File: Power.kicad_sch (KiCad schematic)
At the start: 21 parts, among them U601 HT7463A, U602 BD2243G, U603 MIC5504-3.3YM5

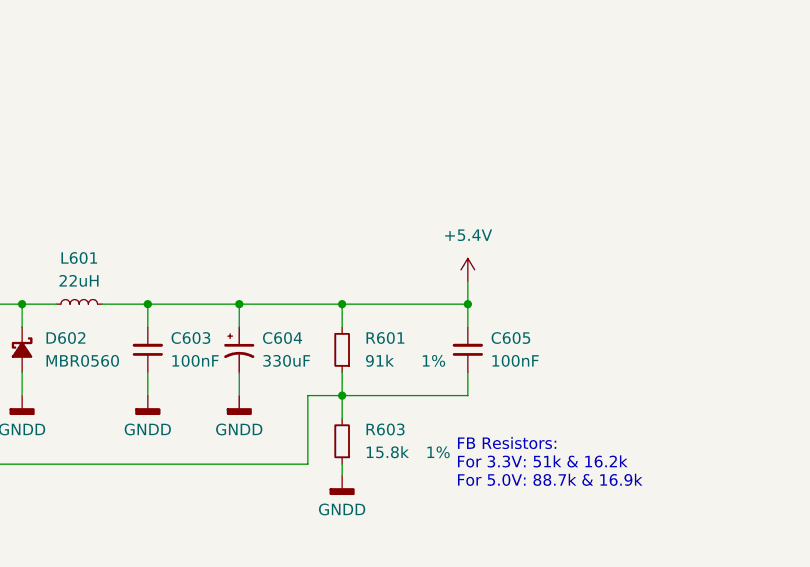
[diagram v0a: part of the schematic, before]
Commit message: Many more vias, improved some routing
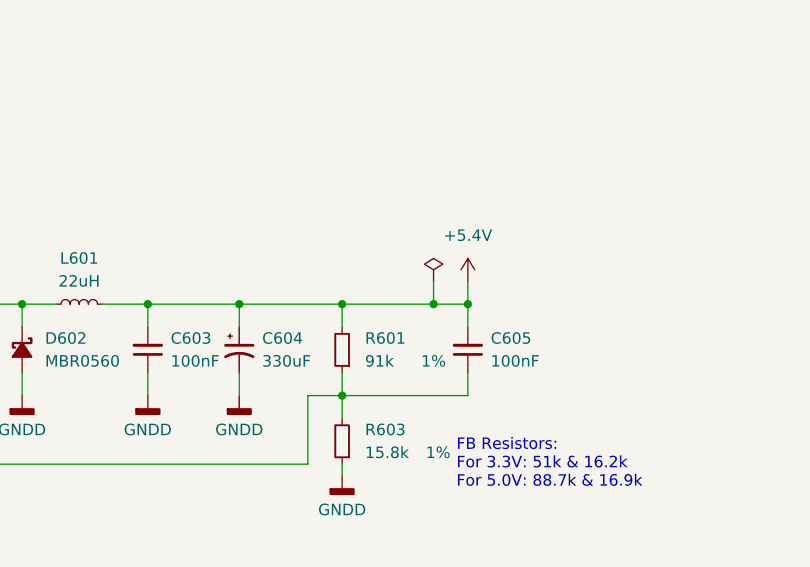
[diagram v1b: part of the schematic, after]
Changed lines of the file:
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@@
+	)
+	(junction
+		(at 173.99 55.88)
+		(diameter 0)
+		(color 0 0 0 0)
 	)
 	(junction
@@
 	(wire
 		(pts
+			(xy 173.99 53.34) (xy 173.99 55.88)
+		)
+		(stroke
+			(width 0)
+			(type default)
+		)
+	)
+	(wire
+		(pts
 			(xy 67.31 95.25) (xy 67.31 90.17)
 		)
@@
 	(wire
 		(pts
+			(xy 173.99 55.88) (xy 177.8 55.88)
+		)
+		(stroke
+			(width 0)
+			(type solid)
+		)
+	)
+	(wire
+		(pts
 			(xy 114.3 106.68) (xy 114.3 109.22)
 		)
@@
 	(wire
 		(pts
-			(xy 163.83 55.88) (xy 177.8 55.88)
+			(xy 163.83 55.88) (xy 173.99 55.88)
 		)
 		(stroke
@@
 					(unit 1)
 				)
+			)
+		)
+	)
+	(symbol
+		(lib_id "power:PWR_FLAG")
+		(at 173.99 53.34 0)
+		(unit 1)
+		(exclude_from_sim no)
+		(in_bom yes)
+		(on_board yes)
+		(dnp no)
+		(fields_autoplaced yes)
+		(property "Reference" "#FLG0601"
+			(at 173.99 51.435 0)
+			(effects
+				(font
+					(size 1.27 1.27)
+				)
+				(hide yes)
+			)
+		)
+		(property "Value" "PWR_FLAG"
+			(at 173.99 48.26 0)
+			(effects
+				(font
+					(size 1.27 1.27)
+				)
+				(hide yes)
+			)
+		)
+		(property "Footprint" ""
+			(at 173.99 53.34 0)
+			(effects
+				(font
+					(size 1.27 1.27)
+				)
+				(hide yes)
+			)
+		)
+		(property "Datasheet" "~"
+			(at 173.99 53.34 0)
+			(effects
+				(font
+					(size 1.27 1.27)
+				)
+				(hide yes)
+			)
+		)
+		(property "Description" "Special symbol for telling ERC where power comes from"
+			(at 173.99 53.34 0)
+			(effects
+				(font
+					(size 1.27 1.27)
+				)
+				(hide yes)
+			)
+		)
+		(pin "1"
+		)
+		(instances
+			(project "ZFTuner"
+				(path "/fdb95973-bff7-44bf-8fa0-11fcc1e3382d/4f4b3f21-035d-41e9-bc50-b9de10321df3"
+					(reference "#FLG0601")
+					(unit 1)
+				)

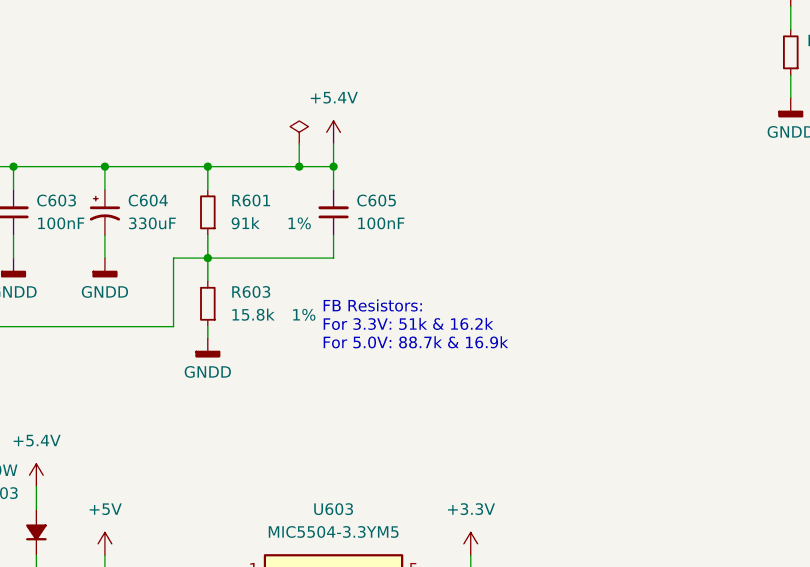
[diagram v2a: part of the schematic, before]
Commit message: Removed unclear text in schematic. Some minor PCB routing improvments. Added name and revision silkscreen
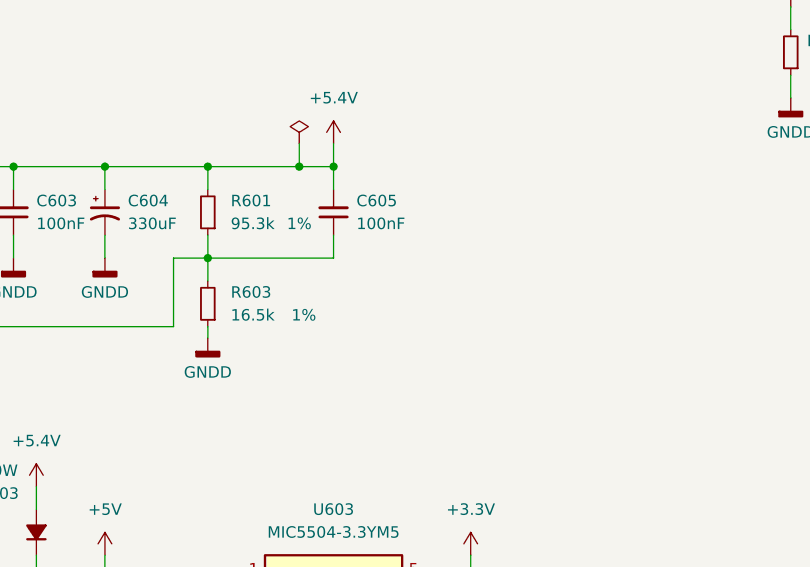
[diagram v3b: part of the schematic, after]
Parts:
- R601: value 91k -> 95.3k
- R603: value 15.8k -> 16.5k
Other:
- note removed: "FB Resistors: For 3.3V: 51k & 16.2k For 5.0V: 88.7k & 16.9k"
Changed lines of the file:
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@@
-		)
-	)
-	(text "FB Resistors:\nFor 3.3V: 51k & 16.2k\nFor 5.0V: 88.7k & 16.9k"
-		(exclude_from_sim no)
-		(at 176.53 76.454 0)
-		(effects
-			(font
-				(size 1.27 1.27)
-			)
-			(justify left bottom)
 		)
 	)
@@
 			)
 		)
-		(property "Value" "91k"
+		(property "Value" "95.3k"
 			(at 166.37 62.2299 0)
 			(effects
@@
 			)
 		)
-		(property "Value" "15.8k"
+		(property "Value" "16.5k"
 			(at 166.37 72.3899 0)
 			(effects

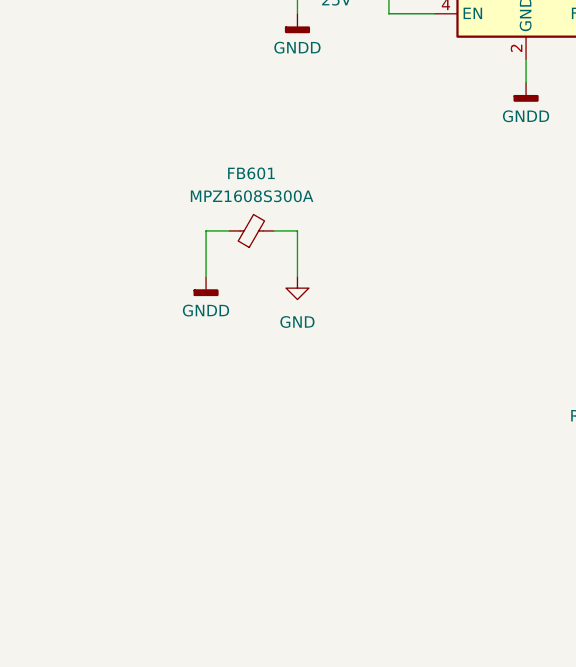
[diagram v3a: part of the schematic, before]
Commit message: Improved grounding
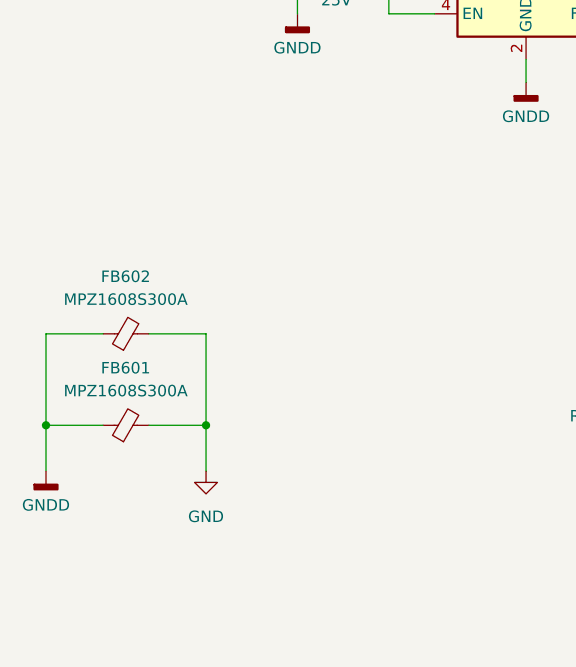
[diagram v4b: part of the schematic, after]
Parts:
- added FB602: MPZ1608S300A, Inductor_SMD:L_0603_1608Metric, symbol Device:FerriteBead_Small
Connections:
- net GND: now also FB602.2
- net GNDD: now also FB602.1
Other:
- moved on the sheet: FB601
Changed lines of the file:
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@@
 	)
 	(junction
+		(at 67.31 111.76)
+		(diameter 0)
+		(color 0 0 0 0)
+	)
+	(junction
 		(at 163.83 66.04)
 		(diameter 0)
@@
 	)
 	(junction
+		(at 49.53 111.76)
+		(diameter 0)
+		(color 0 0 0 0)
+	)
+	(junction
 		(at 87.63 55.88)
 		(diameter 0)
@@
 	(wire
 		(pts
+			(xy 49.53 111.76) (xy 49.53 101.6)
+		)
+		(stroke
+			(width 0)
+			(type default)
+		)
+	)
+	(wire
+		(pts
 			(xy 177.8 53.34) (xy 177.8 55.88)
 		)
@@
 	(wire
 		(pts
-			(xy 67.31 95.25) (xy 67.31 90.17)
+			(xy 49.53 116.84) (xy 49.53 111.76)
 		)
 		(stroke
@@
 	(wire
 		(pts
-			(xy 74.93 90.17) (xy 77.47 90.17)
+			(xy 67.31 101.6) (xy 60.96 101.6)
+		)
+		(stroke
+			(width 0)
+			(type default)
+		)
+	)
+	(wire
+		(pts
+			(xy 60.96 111.76) (xy 67.31 111.76)
 		)
 		(stroke
@@
 	(wire
 		(pts
+			(xy 49.53 101.6) (xy 55.88 101.6)
+		)
+		(stroke
+			(width 0)
+			(type default)
+		)
+	)
+	(wire
+		(pts
 			(xy 120.65 60.96) (xy 123.19 60.96)
 		)
@@
 	(wire
 		(pts
-			(xy 77.47 90.17) (xy 77.47 95.25)
+			(xy 67.31 111.76) (xy 67.31 116.84)
 		)
 		(stroke
@@
 	(wire
 		(pts
+			(xy 67.31 111.76) (xy 67.31 101.6)
+		)
+		(stroke
+			(width 0)
+			(type default)
+		)
+	)
+	(wire
+		(pts
 			(xy 128.27 63.5) (xy 128.27 66.04)
 		)
@@
 	(wire
 		(pts
-			(xy 67.31 90.17) (xy 69.85 90.17)
+			(xy 49.53 111.76) (xy 55.88 111.76)
 		)
 		(stroke
@@
 	(symbol
 		(lib_id "power:GND")
-		(at 77.47 95.25 0)
+		(at 67.31 116.84 0)
 		(unit 1)
 		(exclude_from_sim no)
@@
 		(fields_autoplaced yes)
 		(property "Reference" "#PWR0613"
-			(at 77.47 101.6 0)
+			(at 67.31 123.19 0)
 			(effects
 				(font
@@
 		)
 		(property "Value" "GND"
-			(at 77.47 100.33 0)
+			(at 67.31 121.92 0)
 			(effects
 				(font
@@
 		)
 		(property "Footprint" ""
-			(at 77.47 95.25 0)
+			(at 67.31 116.84 0)
 			(effects
 				(font
@@
 		)
 		(property "Datasheet" ""
-			(at 77.47 95.25 0)
+			(at 67.31 116.84 0)
 			(effects
 				(font
@@
 		)
 		(property "Description" "Power symbol creates a global label with name \"GND\" , ground"
-			(at 77.47 95.25 0)
+			(at 67.31 116.84 0)
 			(effects
 				(font
@@
 	)
 	(symbol
+		(lib_id "Device:FerriteBead_Small")
+		(at 58.42 101.6 90)
+		(unit 1)
+		(exclude_from_sim no)
+		(in_bom yes)
+		(on_board yes)
+		(dnp no)
+		(fields_autoplaced yes)
+		(property "Reference" "FB602"
+			(at 58.3819 95.25 90)
+			(effects
+				(font
+					(size 1.27 1.27)
+				)
+			)
+		)
+		(property "Value" "MPZ1608S300A"
+			(at 58.3819 97.79 90)
+			(effects
+				(font
+					(size 1.27 1.27)
+				)
+			)
+		)
+		(property "Footprint" "Inductor_SMD:L_0603_1608Metric"
+			(at 58.42 103.378 90)
+			(effects
+				(font
+					(size 1.27 1.27)
+				)
+				(hide yes)
+			)
+		)
+		(property "Datasheet" "~"
+			(at 58.42 101.6 0)
+			(effects
+				(font
+					(size 1.27 1.27)
+				)
+				(hide yes)
+			)
+		)
+		(property "Description" "Ferrite bead, small symbol"
+			(at 58.42 101.6 0)
+			(effects
+				(font
+					(size 1.27 1.27)
+				)
+				(hide yes)
+			)
+		)
+		(pin "2"
+		)
+		(pin "1"
+		)
+		(instances
+			(project "ZFTuner"
+				(path "/fdb95973-bff7-44bf-8fa0-11fcc1e3382d/4f4b3f21-035d-41e9-bc50-b9de10321df3"
+					(reference "FB602")
+					(unit 1)
+				)
+			)
+		)
+	)
+	(symbol
 		(lib_id "power:GNDD")
 		(at 152.4 111.76 0)
@@
 	(symbol
 		(lib_id "power:GNDD")
-		(at 67.31 95.25 0)
+		(at 49.53 116.84 0)
 		(unit 1)
 		(exclude_from_sim no)
@@
 		(fields_autoplaced yes)
 		(property "Reference" "#PWR0612"
-			(at 67.31 101.6 0)
+			(at 49.53 123.19 0)
 			(effects
 				(font
@@
 		)
 		(property "Value" "GNDD"
-			(at 67.31 99.06 0)
+			(at 49.53 120.65 0)
 			(effects
 				(font
@@
 		)
 		(property "Footprint" ""
-			(at 67.31 95.25 0)
+			(at 49.53 116.84 0)
 			(effects
 				(font
@@
 		)
 		(property "Datasheet" ""
-			(at 67.31 95.25 0)
+			(at 49.53 116.84 0)
 			(effects
 				(font
@@
 		)
 		(property "Description" "Power symbol creates a global label with name \"GNDD\" , digital ground"
-			(at 67.31 95.25 0)
+			(at 49.53 116.84 0)
 			(effects
 				(font
@@
 	(symbol
 		(lib_id "Device:FerriteBead_Small")
-		(at 72.39 90.17 90)
+		(at 58.42 111.76 90)
 		(unit 1)
 		(exclude_from_sim no)
@@
 		(fields_autoplaced yes)
 		(property "Reference" "FB601"
-			(at 72.3519 83.82 90)
+			(at 58.3819 105.41 90)
 			(effects
 				(font
@@
 		)
 		(property "Value" "MPZ1608S300A"
-			(at 72.3519 86.36 90)
+			(at 58.3819 107.95 90)
 			(effects
 				(font
@@
 		)
 		(property "Footprint" "Inductor_SMD:L_0603_1608Metric"
-			(at 72.39 91.948 90)
+			(at 58.42 113.538 90)
 			(effects
 				(font
@@
 		)
 		(property "Datasheet" "~"
-			(at 72.39 90.17 0)
+			(at 58.42 111.76 0)
 			(effects
 				(font
@@
 		)
 		(property "Description" "Ferrite bead, small symbol"
-			(at 72.39 90.17 0)
+			(at 58.42 111.76 0)
 			(effects
 				(font

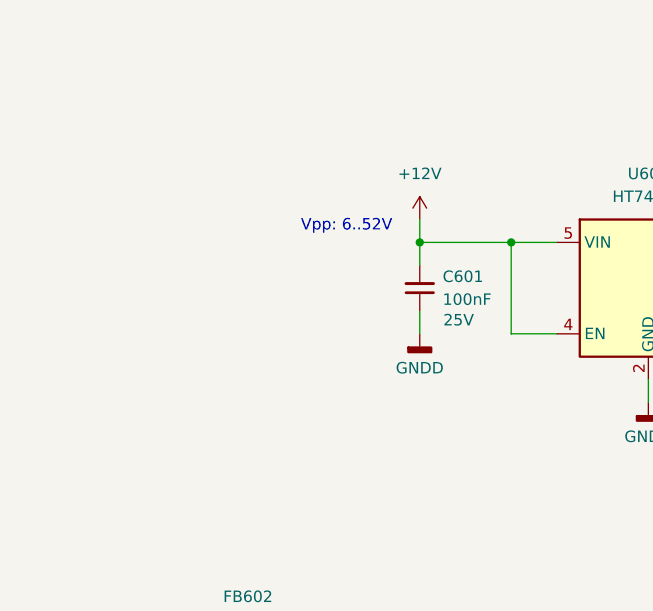
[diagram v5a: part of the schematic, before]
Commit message: Added transistors parts. Added reverse polarity protection, pending adding to layout
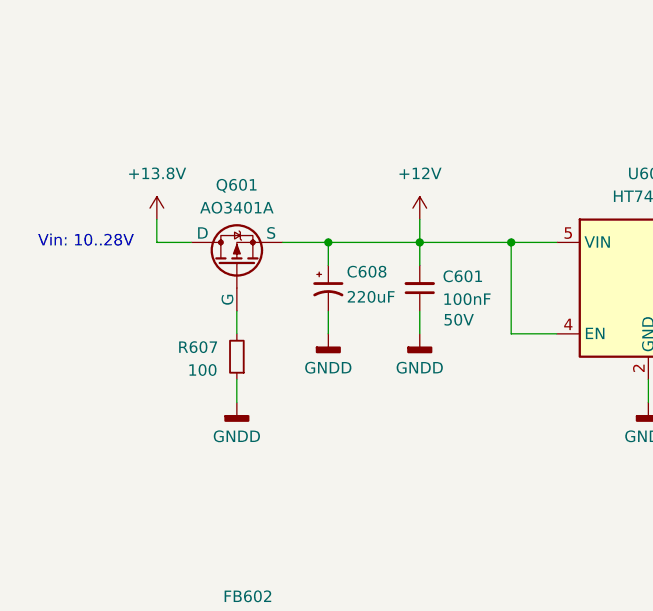
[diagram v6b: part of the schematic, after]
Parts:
- added C608: 220uF, Capacitor_THT:CP_Radial_D10.0mm_P5.00mm, symbol Device:C_Polarized_Small_US
- added Q601: AO3401A, Package_TO_SOT_SMD:SOT-23, symbol Simulation_SPICE:PMOS
- added R607: 100, Resistor_SMD:R_0603_1608Metric, symbol Device:R_Small
- C601: Voltage 25V -> 50V
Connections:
- net +12V: now also C608.1, Q601.3 (S)
- net GNDD: now also C608.2, R607.1
- new net: Q601.2 (G), R607.2
- new net +13.8V: Q601.1 (D)
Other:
- note added: "Vin: 10..28V"
- note removed: "Vpp: 6..52V"
